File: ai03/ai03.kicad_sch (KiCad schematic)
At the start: 3 parts, among them U1 ATmega32U4-A

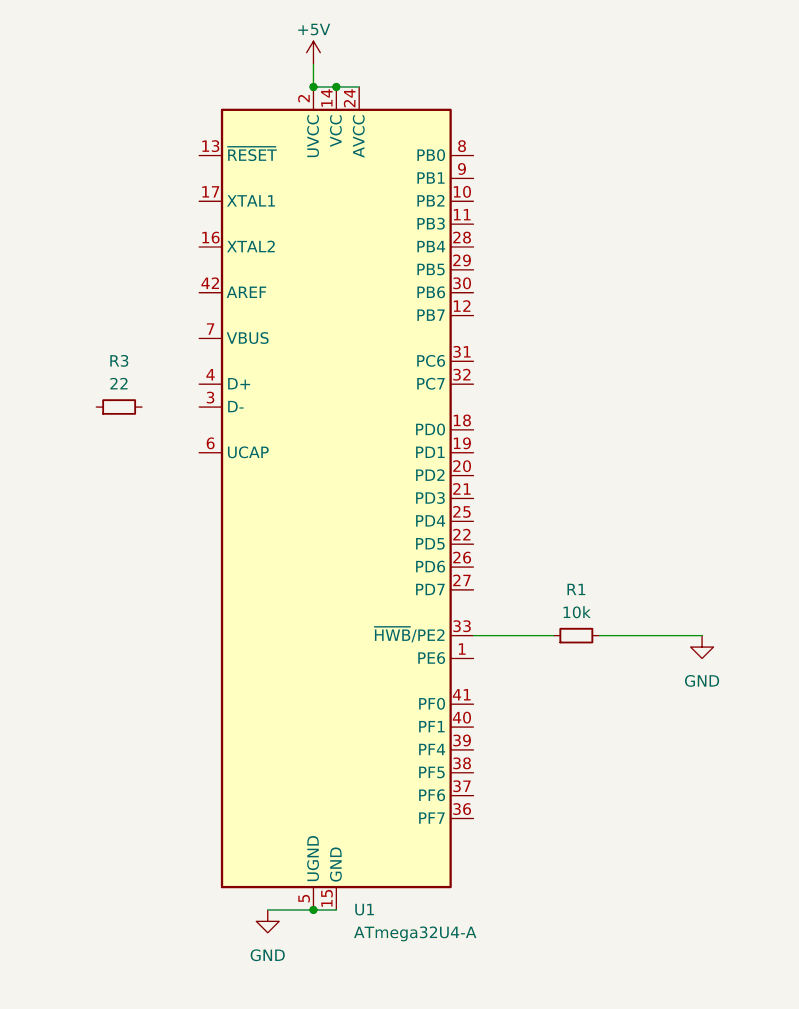
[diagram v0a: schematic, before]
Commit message: Repurposed 'popstar' to be ai03 tutorial. Real popstar PCB design will be in rp2040 folder.
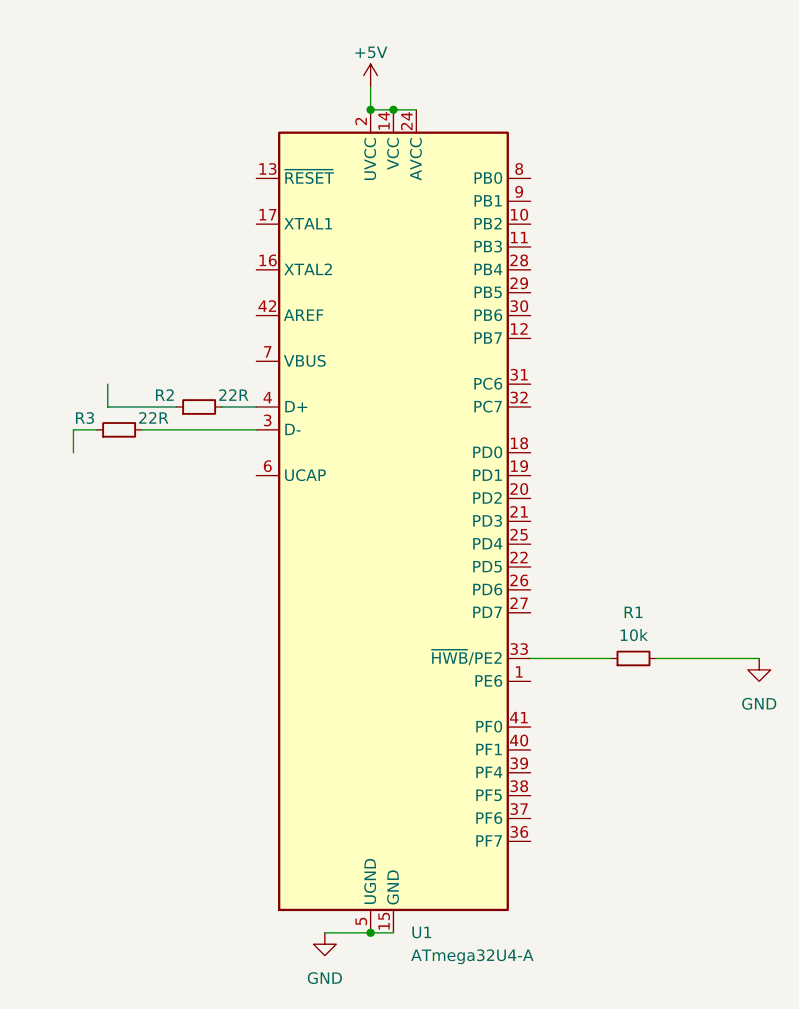
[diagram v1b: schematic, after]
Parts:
- added R2: 22R, symbol Device:R_Small
- R3: value 22 -> 22R
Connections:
- net at U1.3 (D-): now also R3.2
- net at U1.4 (D+): now also R2.2
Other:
- moved on the sheet: R1, R3, U1
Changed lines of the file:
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@@
 (kicad_sch (version 20230121) (generator eeschema)
   (paper "A4")
-  (junction (at 48.26 22.86) (diameter 0) (color 0 0 0 0)
-  )
-  (junction (at 50.8 22.86) (diameter 0) (color 0 0 0 0)
-  )
-  (junction (at 48.26 114.3) (diameter 0) (color 0 0 0 0)
-  )
-  (wire (pts (xy 50.8 22.86) (xy 53.34 22.86))
-    (stroke (width 0) (type default))
-  )
-  (wire (pts (xy 48.26 22.86) (xy 50.8 22.86))
-    (stroke (width 0) (type default))
-  )
-  (wire (pts (xy 66.04 83.82) (xy 74.93 83.82))
-    (stroke (width 0) (type default))
-  )
-  (wire (pts (xy 48.26 114.3) (xy 50.8 114.3))
-    (stroke (width 0) (type default))
-  )
-  (wire (pts (xy 80.01 83.82) (xy 91.44 83.82))
-    (stroke (width 0) (type default))
-  )
-  (wire (pts (xy 43.18 114.3) (xy 48.26 114.3))
-    (stroke (width 0) (type default))
-  )
-  (wire (pts (xy 48.26 20.32) (xy 48.26 22.86))
-    (stroke (width 0) (type default))
-  )
-  (symbol (lib_id "Device:R_Small") (at 77.47 83.82 90) (unit 1)
-    (in_bom yes) (on_board yes) (dnp no) (fields_autoplaced)
-    (property "Reference" "R1" (at 77.47 78.74 90)
-      (effects (font (size 1.27 1.27)))
-    )
-    (property "Value" "10k" (at 77.47 81.28 90)
-      (effects (font (size 1.27 1.27)))
-    )
-    (property "Footprint" "" (at 77.47 83.82 0)
-      (effects (font (size 1.27 1.27)) hide)
-    )
-    (property "Datasheet" "~" (at 77.47 83.82 0)
+  (junction (at 54.61 25.4) (diameter 0) (color 0 0 0 0)
+  )
+  (junction (at 57.15 25.4) (diameter 0) (color 0 0 0 0)
+  )
+  (junction (at 54.61 116.84) (diameter 0) (color 0 0 0 0)
+  )
+  (wire (pts (xy 24.13 60.96) (xy 21.59 60.96))
+    (stroke (width 0) (type default))
+  )
+  (wire (pts (xy 25.4 55.88) (xy 25.4 58.42))
+    (stroke (width 0) (type default))
+  )
+  (wire (pts (xy 57.15 25.4) (xy 59.69 25.4))
+    (stroke (width 0) (type default))
+  )
+  (wire (pts (xy 54.61 25.4) (xy 57.15 25.4))
+    (stroke (width 0) (type default))
+  )
+  (wire (pts (xy 21.59 60.96) (xy 21.59 63.5))
+    (stroke (width 0) (type default))
+  )
+  (wire (pts (xy 25.4 58.42) (xy 33.02 58.42))
+    (stroke (width 0) (type default))
+  )
+  (wire (pts (xy 29.21 60.96) (xy 41.91 60.96))
+    (stroke (width 0) (type default))
+  )
+  (wire (pts (xy 72.39 86.36) (xy 81.28 86.36))
+    (stroke (width 0) (type default))
+  )
+  (wire (pts (xy 54.61 116.84) (xy 57.15 116.84))
+    (stroke (width 0) (type default))
+  )
+  (wire (pts (xy 86.36 86.36) (xy 97.79 86.36))
+    (stroke (width 0) (type default))
+  )
+  (wire (pts (xy 49.53 116.84) (xy 54.61 116.84))
+    (stroke (width 0) (type default))
+  )
+  (wire (pts (xy 38.1 58.42) (xy 41.91 58.42))
+    (stroke (width 0) (type default))
+  )
+  (wire (pts (xy 54.61 22.86) (xy 54.61 25.4))
+    (stroke (width 0) (type default))
+  )
+  (symbol (lib_id "Device:R_Small") (at 83.82 86.36 90) (unit 1)
+    (in_bom yes) (on_board yes) (dnp no) (fields_autoplaced)
+    (property "Reference" "R1" (at 83.82 81.28 90)
+      (effects (font (size 1.27 1.27)))
+    )
+    (property "Value" "10k" (at 83.82 83.82 90)
+      (effects (font (size 1.27 1.27)))
+    )
+    (property "Footprint" "" (at 83.82 86.36 0)
+      (effects (font (size 1.27 1.27)) hide)
+    )
+    (property "Datasheet" "~" (at 83.82 86.36 0)
       (effects (font (size 1.27 1.27)) hide)
     )
@@
     )
   )
-  (symbol (lib_id "MCU_Microchip_ATmega:ATmega32U4-A") (at 50.8 68.58 0) (unit 1)
-    (in_bom yes) (on_board yes) (dnp no) (fields_autoplaced)
-    (property "Reference" "U1" (at 52.7559 114.3 0)
+  (symbol (lib_id "MCU_Microchip_ATmega:ATmega32U4-A") (at 57.15 71.12 0) (unit 1)
+    (in_bom yes) (on_board yes) (dnp no) (fields_autoplaced)
+    (property "Reference" "U1" (at 59.1059 116.84 0)
       (effects (font (size 1.27 1.27)) (justify left))
     )
-    (property "Value" "ATmega32U4-A" (at 52.7559 116.84 0)
+    (property "Value" "ATmega32U4-A" (at 59.1059 119.38 0)
       (effects (font (size 1.27 1.27)) (justify left))
     )
-    (property "Footprint" "Package_QFP:TQFP-44_10x10mm_P0.8mm" (at 50.8 68.58 0)
+    (property "Footprint" "Package_QFP:TQFP-44_10x10mm_P0.8mm" (at 57.15 71.12 0)
       (effects (font (size 1.27 1.27) italic) hide)
     )
-    (property "Datasheet" "http://ww1.microchip.com/downloads/en/DeviceDoc/Atmel-7766-8-bit-AVR-ATmega16U4-32U4_Datasheet.pdf" (at 50.8 68.58 0)
+    (property "Datasheet" "http://ww1.microchip.com/downloads/en/DeviceDoc/Atmel-7766-8-bit-AVR-ATmega16U4-32U4_Datasheet.pdf" (at 57.15 71.12 0)
       (effects (font (size 1.27 1.27)) hide)
     )
@@
     )
   )
-  (symbol (lib_id "power:GND") (at 91.44 83.82 0) (unit 1)
-    (in_bom yes) (on_board yes) (dnp no) (fields_autoplaced)
-    (property "Reference" "#PWR03" (at 91.44 90.17 0)
-      (effects (font (size 1.27 1.27)) hide)
-    )
-    (property "Value" "GND" (at 91.44 88.9 0)
-      (effects (font (size 1.27 1.27)))
-    )
-    (property "Footprint" "" (at 91.44 83.82 0)
-      (effects (font (size 1.27 1.27)) hide)
-    )
-    (property "Datasheet" "" (at 91.44 83.82 0)
+  (symbol (lib_id "power:GND") (at 97.79 86.36 0) (unit 1)
+    (in_bom yes) (on_board yes) (dnp no) (fields_autoplaced)
+    (property "Reference" "#PWR03" (at 97.79 92.71 0)
+      (effects (font (size 1.27 1.27)) hide)
+    )
+    (property "Value" "GND" (at 97.79 91.44 0)
+      (effects (font (size 1.27 1.27)))
+    )
+    (property "Footprint" "" (at 97.79 86.36 0)
+      (effects (font (size 1.27 1.27)) hide)
+    )
+    (property "Datasheet" "" (at 97.79 86.36 0)
       (effects (font (size 1.27 1.27)) hide)
     )
@@
     )
   )
-  (symbol (lib_id "power:+5V") (at 48.26 20.32 0) (unit 1)
-    (in_bom yes) (on_board yes) (dnp no) (fields_autoplaced)
-    (property "Reference" "#PWR01" (at 48.26 24.13 0)
-      (effects (font (size 1.27 1.27)) hide)
-    )
-    (property "Value" "+5V" (at 48.26 16.51 0)
-      (effects (font (size 1.27 1.27)))
-    )
-    (property "Footprint" "" (at 48.26 20.32 0)
-      (effects (font (size 1.27 1.27)) hide)
-    )
-    (property "Datasheet" "" (at 48.26 20.32 0)
+  (symbol (lib_id "Device:R_Small") (at 35.56 58.42 90) (unit 1)
+    (in_bom yes) (on_board yes) (dnp no)
+    (property "Reference" "R2" (at 31.75 57.15 90)
+      (effects (font (size 1.27 1.27)))
+    )
+    (property "Value" "22R" (at 39.37 57.15 90)
+      (effects (font (size 1.27 1.27)))
+    )
+    (property "Footprint" "" (at 35.56 58.42 0)
+      (effects (font (size 1.27 1.27)) hide)
+    )
+    (property "Datasheet" "~" (at 35.56 58.42 0)
+      (effects (font (size 1.27 1.27)) hide)
+    )
+    (pin "1")
+    (pin "2")
+    (instances
+      (project "popstar"
+        (path "/38a1a9ff-9c00-4248-947e-eb94ab6d8a39"
+          (reference "R2") (unit 1)
+        )
+      )
+    )
+  )
+  (symbol (lib_id "power:+5V") (at 54.61 22.86 0) (unit 1)
+    (in_bom yes) (on_board yes) (dnp no) (fields_autoplaced)
+    (property "Reference" "#PWR01" (at 54.61 26.67 0)
+      (effects (font (size 1.27 1.27)) hide)
+    )
+    (property "Value" "+5V" (at 54.61 19.05 0)
+      (effects (font (size 1.27 1.27)))
+    )
+    (property "Footprint" "" (at 54.61 22.86 0)
+      (effects (font (size 1.27 1.27)) hide)
+    )
+    (property "Datasheet" "" (at 54.61 22.86 0)
       (effects (font (size 1.27 1.27)) hide)
     )
@@
     )
   )
-  (symbol (lib_id "Device:R_Small") (at 26.67 58.42 90) (unit 1)
-    (in_bom yes) (on_board yes) (dnp no) (fields_autoplaced)
-    (property "Reference" "R3" (at 26.67 53.34 90)
-      (effects (font (size 1.27 1.27)))
-    )
-    (property "Value" "22" (at 26.67 55.88 90)
-      (effects (font (size 1.27 1.27)))
-    )
-    (property "Footprint" "" (at 26.67 58.42 0)
-      (effects (font (size 1.27 1.27)) hide)
-    )
-    (property "Datasheet" "~" (at 26.67 58.42 0)
+  (symbol (lib_id "Device:R_Small") (at 26.67 60.96 90) (unit 1)
+    (in_bom yes) (on_board yes) (dnp no)
+    (property "Reference" "R3" (at 22.86 59.69 90)
+      (effects (font (size 1.27 1.27)))
+    )
+    (property "Value" "22R" (at 30.48 59.69 90)
+      (effects (font (size 1.27 1.27)))
+    )
+    (property "Footprint" "" (at 26.67 60.96 0)
+      (effects (font (size 1.27 1.27)) hide)
+    )
+    (property "Datasheet" "~" (at 26.67 60.96 0)
       (effects (font (size 1.27 1.27)) hide)
     )
@@
     )
   )
-  (symbol (lib_id "power:GND") (at 43.18 114.3 0) (unit 1)
-    (in_bom yes) (on_board yes) (dnp no) (fields_autoplaced)
-    (property "Reference" "#PWR02" (at 43.18 120.65 0)
-      (effects (font (size 1.27 1.27)) hide)
-    )
-    (property "Value" "GND" (at 43.18 119.38 0)
-      (effects (font (size 1.27 1.27)))
-    )
-    (property "Footprint" "" (at 43.18 114.3 0)
-      (effects (font (size 1.27 1.27)) hide)
-    )
-    (property "Datasheet" "" (at 43.18 114.3 0)
-      (effects (font (size 1.27 1.27)) hide)
-    )
+  (symbol (lib_id "power:GND") (at 49.53 116.84 0) (unit 1)
+    (in_bom yes) (on_board yes) (dnp no) (fields_autoplaced)
+    (property "Reference" "#PWR02" (at 49.53 123.19 0)
+      (effects (font (size 1.27 1.27)) hide)
+    )
+    (property "Value" "GND" (at 49.53 121.92 0)
+      (effects (font (size 1.27 1.27)))
+    )
+    (property "Footprint" "" (at 49.53 116.84 0)
+      (effects (font (size 1.27 1.27)) hide)
+    )
+    (property "Datasheet" "" (at 49.53 116.84 0)
+      (effects (font (size 1.27 1.27)) hide)
+    )

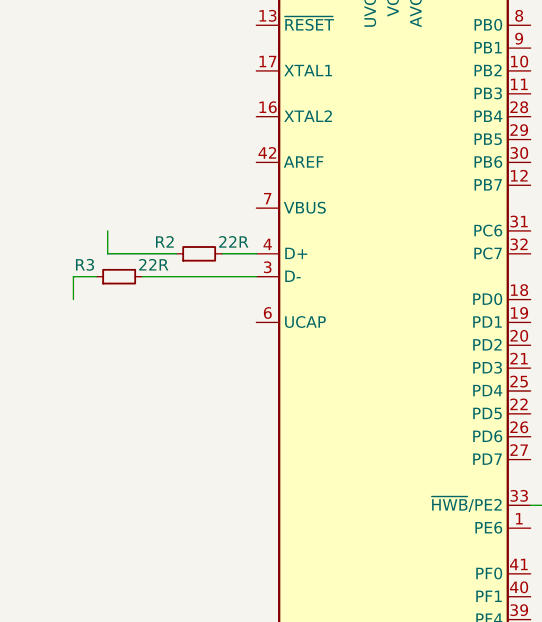
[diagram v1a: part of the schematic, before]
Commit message: Renamed popstar-rp2040 => reference rp2040. Created an actual dir for popstar rp2040 design.
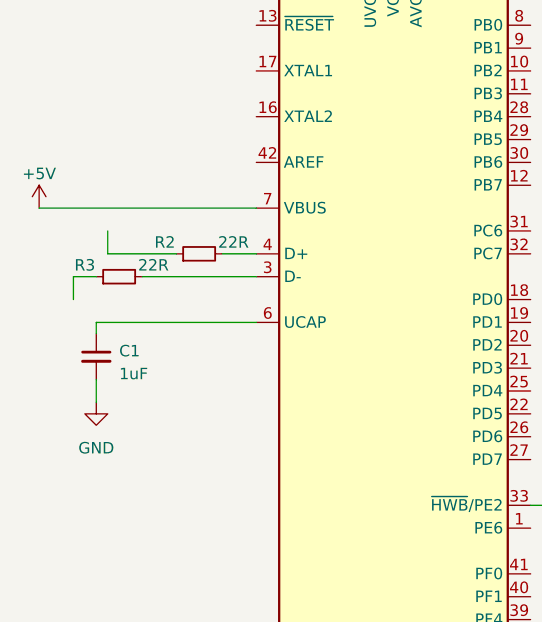
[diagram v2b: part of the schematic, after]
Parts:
- added C1: 1uF, symbol Device:C_Small
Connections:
- net +5V: now also U1.7 (VBUS)
- net GND: now also C1.2
- net at U1.6 (UCAP): now also C1.1
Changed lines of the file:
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@@
   (junction (at 54.61 116.84) (diameter 0) (color 0 0 0 0)
   )
+  (wire (pts (xy 41.91 66.04) (xy 24.13 66.04))
+    (stroke (width 0) (type default))
+  )
   (wire (pts (xy 24.13 60.96) (xy 21.59 60.96))
     (stroke (width 0) (type default))
@@
     (stroke (width 0) (type default))
   )
+  (wire (pts (xy 24.13 66.04) (xy 24.13 67.31))
+    (stroke (width 0) (type default))
+  )
   (wire (pts (xy 21.59 60.96) (xy 21.59 63.5))
     (stroke (width 0) (type default))
@@
     (stroke (width 0) (type default))
   )
+  (wire (pts (xy 17.78 53.34) (xy 41.91 53.34))
+    (stroke (width 0) (type default))
+  )
   (wire (pts (xy 86.36 86.36) (xy 97.79 86.36))
     (stroke (width 0) (type default))
@@
     (stroke (width 0) (type default))
   )
+  (wire (pts (xy 24.13 72.39) (xy 24.13 74.93))
+    (stroke (width 0) (type default))
+  )
   (wire (pts (xy 38.1 58.42) (xy 41.91 58.42))
     (stroke (width 0) (type default))
@@
     (stroke (width 0) (type default))
   )
+  (symbol (lib_id "Device:C_Small") (at 24.13 69.85 0) (unit 1)
+    (in_bom yes) (on_board yes) (dnp no) (fields_autoplaced)
+    (property "Reference" "C1" (at 26.67 69.2213 0)
+      (effects (font (size 1.27 1.27)) (justify left))
+    )
+    (property "Value" "1uF" (at 26.67 71.7613 0)
+      (effects (font (size 1.27 1.27)) (justify left))
+    )
+    (property "Footprint" "" (at 24.13 69.85 0)
+      (effects (font (size 1.27 1.27)) hide)
+    )
+    (property "Datasheet" "~" (at 24.13 69.85 0)
+      (effects (font (size 1.27 1.27)) hide)
+    )
+    (pin "1")
+    (pin "2")
+    (instances
+      (project "ai03"
+        (path "/38a1a9ff-9c00-4248-947e-eb94ab6d8a39"
+          (reference "C1") (unit 1)
+        )
+      )
+    )
+  )
   (symbol (lib_id "Device:R_Small") (at 83.82 86.36 90) (unit 1)
     (in_bom yes) (on_board yes) (dnp no) (fields_autoplaced)
@@
     (pin "2")
     (instances
-      (project "popstar"
+      (project "ai03"
         (path "/38a1a9ff-9c00-4248-947e-eb94ab6d8a39"
           (reference "R1") (unit 1)
@@
     (pin "9")
     (instances
-      (project "popstar"
+      (project "ai03"
         (path "/38a1a9ff-9c00-4248-947e-eb94ab6d8a39"
           (reference "U1") (unit 1)
@@
     (pin "1")
     (instances
-      (project "popstar"
+      (project "ai03"
         (path "/38a1a9ff-9c00-4248-947e-eb94ab6d8a39"
           (reference "#PWR03") (unit 1)
@@
     (pin "2")
     (instances
-      (project "popstar"
+      (project "ai03"
         (path "/38a1a9ff-9c00-4248-947e-eb94ab6d8a39"
           (reference "R2") (unit 1)
@@
     (pin "1")
     (instances
-      (project "popstar"
+      (project "ai03"
         (path "/38a1a9ff-9c00-4248-947e-eb94ab6d8a39"
           (reference "#PWR01") (unit 1)
@@
     (pin "2")
     (instances
-      (project "popstar"
+      (project "ai03"
         (path "/38a1a9ff-9c00-4248-947e-eb94ab6d8a39"
           (reference "R3") (unit 1)
@@
     )
   )
+  (symbol (lib_id "power:GND") (at 24.13 74.93 0) (unit 1)
+    (in_bom yes) (on_board yes) (dnp no) (fields_autoplaced)
+    (property "Reference" "#PWR04" (at 24.13 81.28 0)
+      (effects (font (size 1.27 1.27)) hide)
+    )
+    (property "Value" "GND" (at 24.13 80.01 0)
+      (effects (font (size 1.27 1.27)))
+    )
+    (property "Footprint" "" (at 24.13 74.93 0)
+      (effects (font (size 1.27 1.27)) hide)
+    )
+    (property "Datasheet" "" (at 24.13 74.93 0)
+      (effects (font (size 1.27 1.27)) hide)
+    )
+    (pin "1")
+    (instances
+      (project "ai03"
+        (path "/38a1a9ff-9c00-4248-947e-eb94ab6d8a39"
+          (reference "#PWR04") (unit 1)
+        )
+      )
+    )
+  )
+  (symbol (lib_id "power:+5V") (at 17.78 53.34 0) (unit 1)
+    (in_bom yes) (on_board yes) (dnp no) (fields_autoplaced)
+    (property "Reference" "#PWR05" (at 17.78 57.15 0)
+      (effects (font (size 1.27 1.27)) hide)
+    )
+    (property "Value" "+5V" (at 17.78 49.53 0)
+      (effects (font (size 1.27 1.27)))
+    )
+    (property "Footprint" "" (at 17.78 53.34 0)
+      (effects (font (size 1.27 1.27)) hide)
+    )
+    (property "Datasheet" "" (at 17.78 53.34 0)
+      (effects (font (size 1.27 1.27)) hide)
+    )
+    (pin "1")
+    (instances
+      (project "ai03"
+        (path "/38a1a9ff-9c00-4248-947e-eb94ab6d8a39"
+          (reference "#PWR05") (unit 1)
+        )
+      )
+    )
+  )
   (symbol (lib_id "power:GND") (at 49.53 116.84 0) (unit 1)
     (in_bom yes) (on_board yes) (dnp no) (fields_autoplaced)
@@
     (pin "1")
     (instances
-      (project "popstar"
+      (project "ai03"
         (path "/38a1a9ff-9c00-4248-947e-eb94ab6d8a39"
           (reference "#PWR02") (unit 1)
